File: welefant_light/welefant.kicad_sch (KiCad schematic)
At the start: 95 parts, among them J1 Conn_01x02, J2 Conn_02x7_Odd_Even, J3 Conn_02x6_Odd_Even, Q1 AO3401A, Q2 AO3401A, Q3 AO3401A, SW1 ON-OFF, SW2 RESET, SW3 BOOT, SW4 GPIO33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

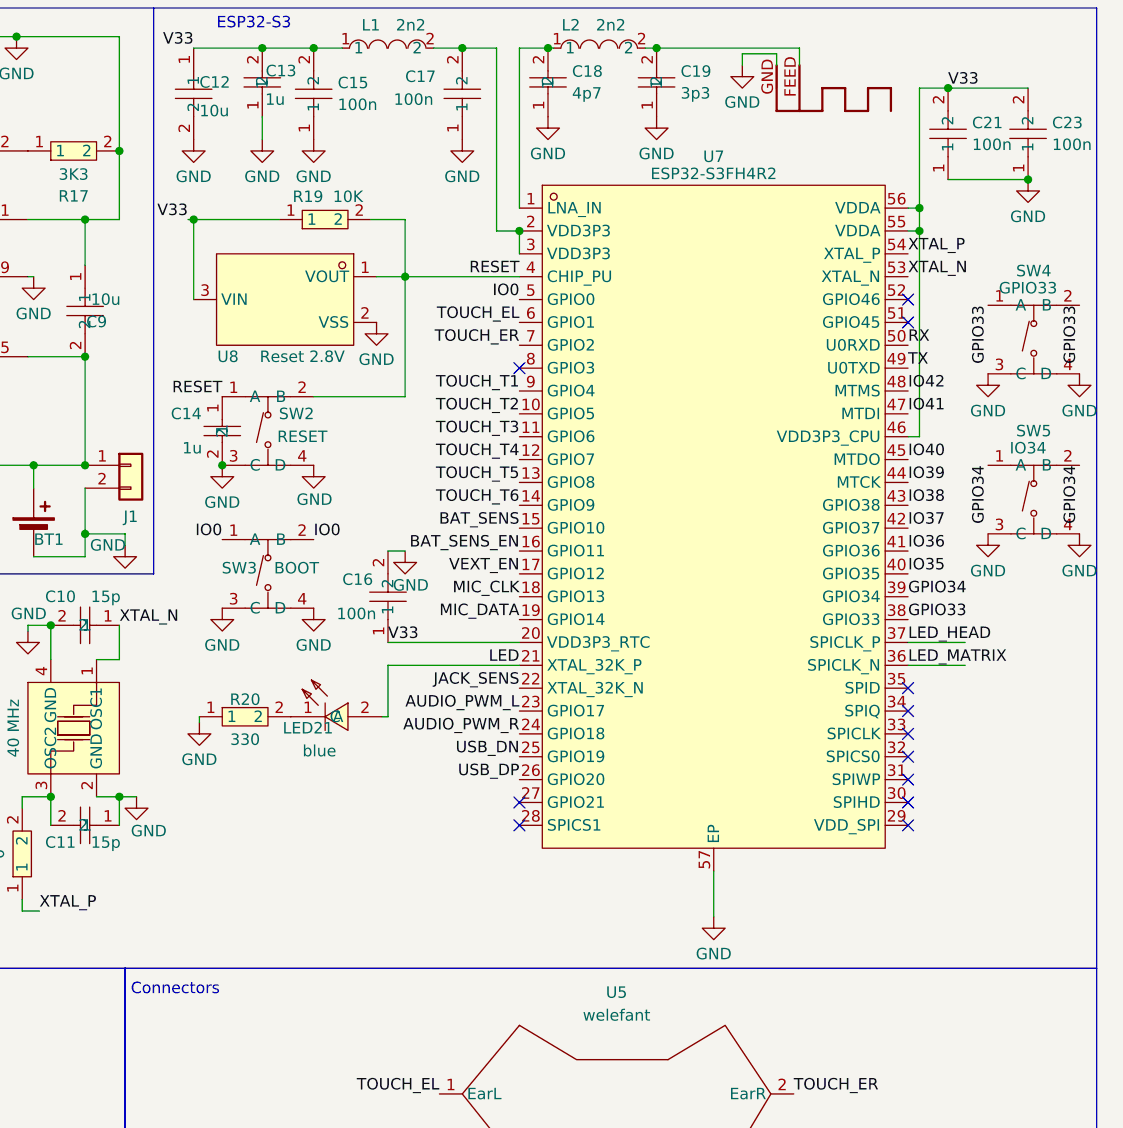
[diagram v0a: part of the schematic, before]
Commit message: Revert "use S3FH4R2 / remove flash chip"
This reverts commit b0f4cc23a485e26b2c676c6cda33926215215541.
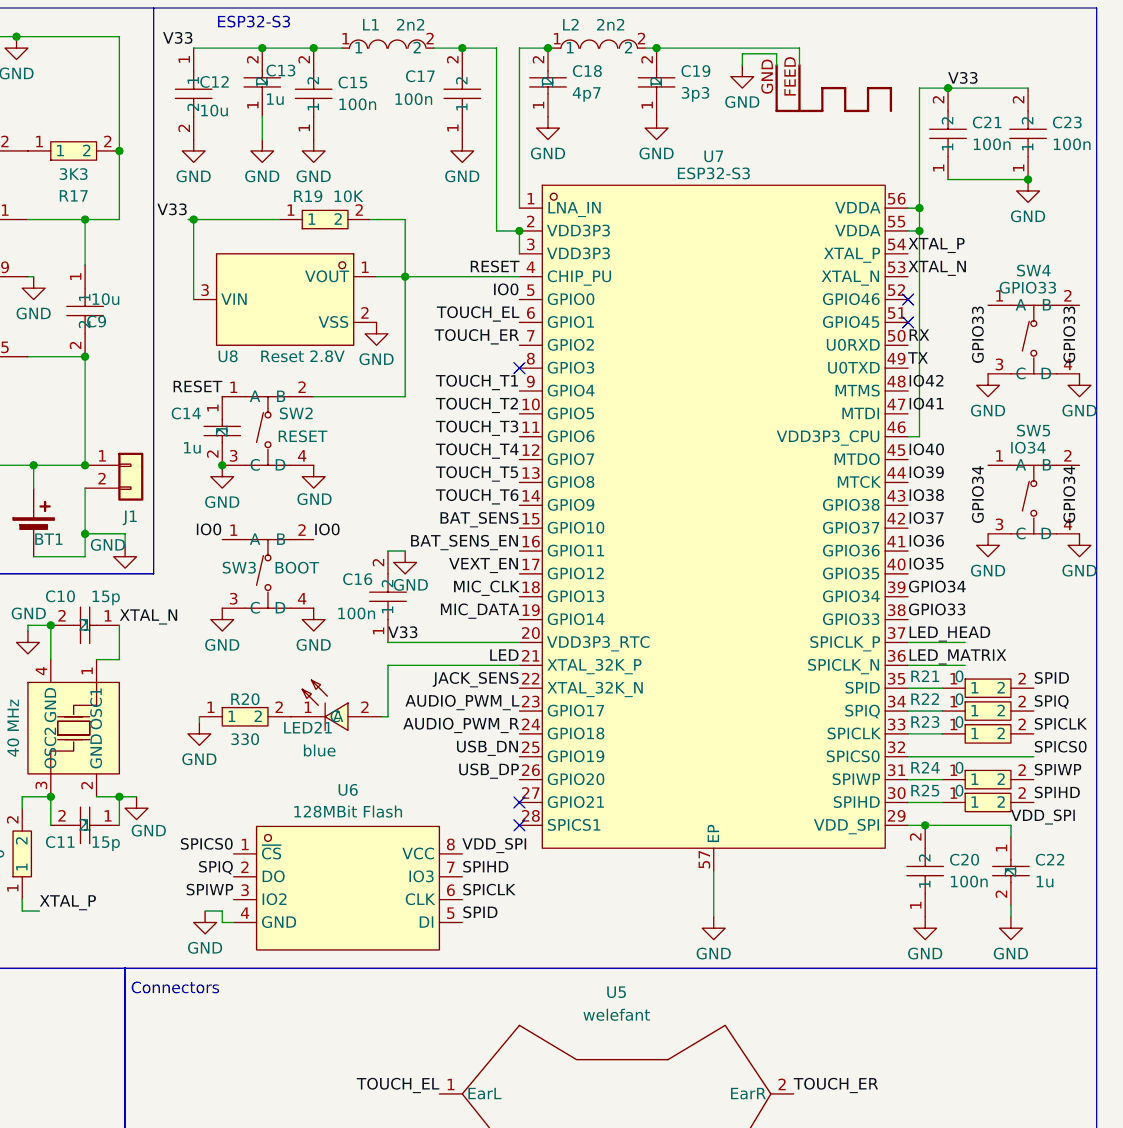
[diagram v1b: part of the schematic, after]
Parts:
- added C20: 100n, easyeda2kicad:C0603, symbol easyeda2kicad:CC0603KRX7R9BB104
- added C22: 1u, easyeda2kicad:C0603, symbol easyeda2kicad:CL10A105KB8NNNC
- added R21, R22, R23, R24, R25: 0, easyeda2kicad:R0603, symbol easyeda2kicad:0603WAF0000T5E
- added U6: 128MBit Flash, easyeda2kicad:SOIC-8_L5.3-W5.3-P1.27-LS8.0-BL, symbol easyeda2kicad:W25Q128JVSIQTR
- U7: value ESP32-S3FH4R2 -> ESP32-S3; LCSC Part C3013940 -> C2913192
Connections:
- net GND: now also C20.1, C22.2, U6.4 (GND)
- net VDD_SPI: now reaches U7.29 (VDD_SPI)
- net VDD_SPI: now also C20.2, C22.1, U6.8 (VCC)
- net at U7.30 (SPIHD): now also R25.1
- net at U7.31 (SPIWP): now also R24.1
- net SPICS0: now reaches U7.32 (SPICS0)
- net SPICS0: now also U6.1 (~{CS})
- net at U7.33 (SPICLK): now also R23.1
- net at U7.34 (SPIQ): now also R22.1
- net at U7.35 (SPID): now also R21.1
- new net SPICLK: R23.2, U6.6 (CLK)
- new net SPID: R21.2, U6.5 (DI)
- new net SPIHD: R25.2, U6.7 (IO3)
- new net SPIQ: R22.2, U6.2 (DO)
- new net SPIWP: R24.2, U6.3 (IO2)
- no-connect marks 28 -> 21
